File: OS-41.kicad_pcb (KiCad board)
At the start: 4 copper layers, 45.2 x 55.8 mm, 74 parts, among them J1 Conn_01x02_Pin, J2 Conn_01x02_Pin, J3 Conn_01x02_Pin, J4 Conn_Coaxial, J5 Conn_01x02_Pin, J6 USB_B_Micro, J7 Conn_01x09_Pin, SW2 TS-1187A-B-A-B, SW3 TS-1187A-B-A-B, U1 GPS1003, U10 W25Q128JVS, U2 SI4432-B1-FMR, U3 MCP1640x-xCHY, U4 ATGM336H-5N31, U5 DS18B20, U6 BMP390L, U7 RP2040, U8 ABM8-272-T3_C20625731, U9 AMS1117-3.3, X1 SMD-3225_4P 30.000MHZ 10PF

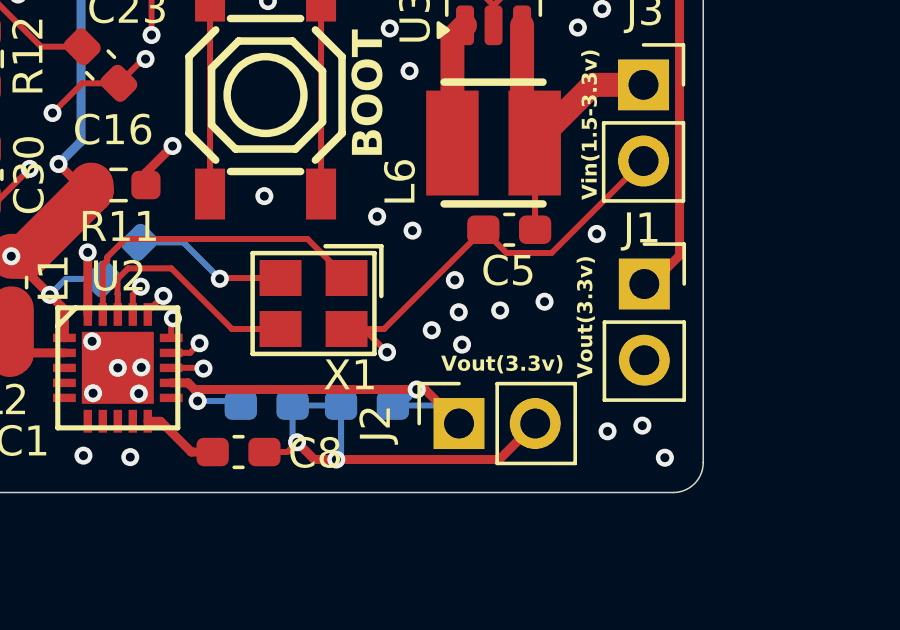
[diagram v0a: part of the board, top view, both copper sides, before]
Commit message: add polarity
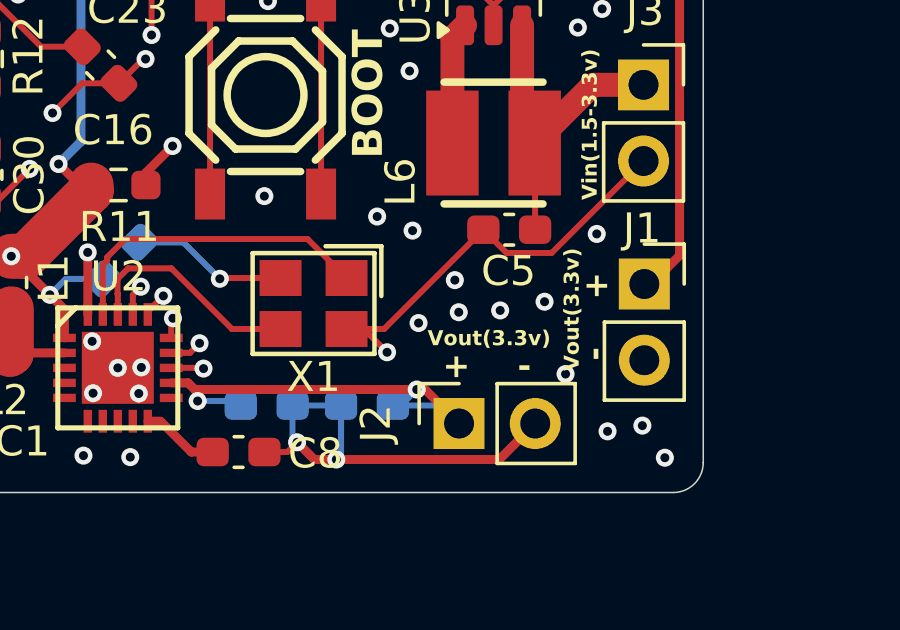
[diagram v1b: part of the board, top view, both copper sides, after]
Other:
- board text added: "+"
- board text added: "-"
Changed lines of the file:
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@@
 		(at 125 122.15 180)
 		(property "Reference" "X1"
-			(at -1.225 -2.4 0)
+			(at 0 -2.45 0)
 			(layer "F.SilkS")
 			(effects
@@
 		(layer "Edge.Cuts")
 	)
+	(gr_text "+"
+		(at 132.9 115.7 0)
+		(layer "B.SilkS")
+		(effects
+			(font
+				(size 1.5 1.5)
+				(thickness 0.3)
+				(bold yes)
+			)
+			(justify left bottom)
+		)
+	)
+	(gr_text "-"
+		(at 134.8 118.5 90)
+		(layer "B.SilkS")
+		(effects
+			(font
+				(size 1.5 1.5)
+				(thickness 0.3)
+				(bold yes)
+			)
+			(justify left bottom)
+		)
+	)
 	(gr_text "G13"
 		(at 93.2 109.1 -90)
@@
 	)
 	(gr_text "Vout(3.3v)"
-		(at 129.25 124.45 0)
+		(at 128.8 123.6 0)
 		(layer "F.SilkS")
 		(effects
@@
 	)
 	(gr_text "Vout(3.3v)"
-		(at 134.35 124.65 90)
+		(at 133.9 124.4 90)
 		(layer "F.SilkS")
 		(effects
@@
 		)
 	)
+	(gr_text "+"
+		(at 134 121.1 -90)
+		(layer "F.SilkS")
+		(effects
+			(font
+				(size 0.8 0.8)
+				(thickness 0.15)
+				(bold yes)
+			)
+			(justify left bottom)
+		)
+	)
 	(gr_text "G"
 		(at 104.95 111.39 0)
@@
 		)
 	)
+	(gr_text "-"
+		(at 134 123.6 -90)
+		(layer "F.SilkS")
+		(effects
+			(font
+				(size 0.8 0.8)
+				(thickness 0.15)
+				(bold yes)
+			)
+			(justify left bottom)
+		)
+	)
 	(gr_text "R"
 		(at 104.91 113.5 0)
@@
 		)
 	)
+	(gr_text "+"
+		(at 129.3 124.7 0)
+		(layer "F.SilkS")
+		(effects
+			(font
+				(size 0.8 0.8)
+				(thickness 0.15)
+				(bold yes)
+			)
+			(justify left bottom)
+		)
+	)
 	(gr_text "G12"
 		(at 93.2 106.4 -90)
@@
 		)
 	)
+	(gr_text "-"
+		(at 131.8 124.7 0)
+		(layer "F.SilkS")
+		(effects
+			(font
+				(size 0.8 0.8)
+				(thickness 0.15)
+				(bold yes)
+			)
+			(justify left bottom)
+		)
+	)
 	(gr_text "ERR"
 		(at 103.31 115.61 0)
@@
 	)
 	(via
-		(at 128.94 123.04)
+		(at 128.5 122.8)
 		(size 0.6)
 		(drill 0.3)
@@
 	)
 	(via
-		(at 129.95 123.52)
+		(at 133.4 124.5)
 		(size 0.6)
 		(drill 0.3)

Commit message: Fix some important things
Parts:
- added C15: 100nF, Capacitor_SMD:C_0603_1608Metric_Pad1.08x0.95mm_HandSolder, B.Cu at (100.8, 116.2)
- added R13: 4.7k, Resistor_SMD:R_0603_1608Metric_Pad0.98x0.95mm_HandSolder, B.Cu at (121.5, 99.1)
- added R14: 4.7k, Resistor_SMD:R_0603_1608Metric_Pad0.98x0.95mm_HandSolder, B.Cu at (123.3, 109.8)
- added R5: 10k, Resistor_SMD:R_0603_1608Metric_Pad0.98x0.95mm_HandSolder, F.Cu at (98.6, 108.4)
- R2: value 12k -> 10k
- renumbered C15 to C16, C16 to C17, C17 to C18, C18 to C19, C19 to C20, C20 to C21, C21 to C22, C22 to C23, C23 to C24, C24 to C25, C25 to C26, C26 to C27, C27 to C28, C28 to C29, C29 to C30, C30 to C31, C31 to C32, R9 to R10, R10 to R11, R11 to R12, R12 to R15, R13 to R16, R14 to R17, R5 to R6, R6 to R7, R7 to R8, R8 to R9, SW2 to SW1, SW3 to SW2
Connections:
- U7 pad 34: unconnected-(U7-GPIO22-Pad34) -> DQ
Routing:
- net DQ: track 6.00 -> 28.5 mm, vias 0 -> 2
- net VCC: track 225.5 -> 238.4 mm, vias 17 -> 18
- net SCL: track 8.61 -> 15.5 mm, vias 2 -> 3
- net RESET: track 25.8 -> 30.6 mm, vias 2 -> 3
- net GND: track 333.1 -> 337.6 mm, vias 156 -> 157
- net SDA: track 9.70 -> 11.5 mm

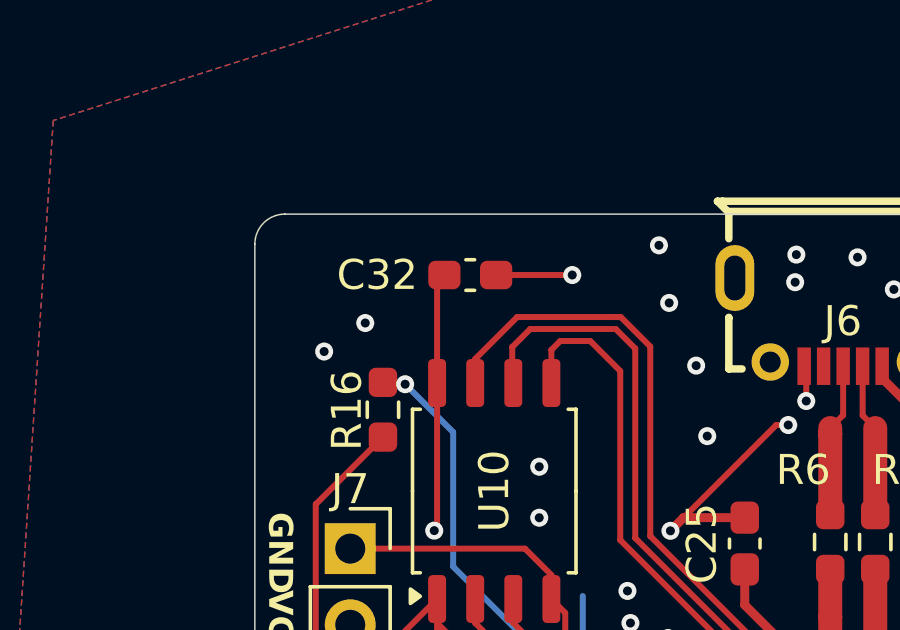
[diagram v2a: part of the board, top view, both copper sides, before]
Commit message: Rotate a capacitor
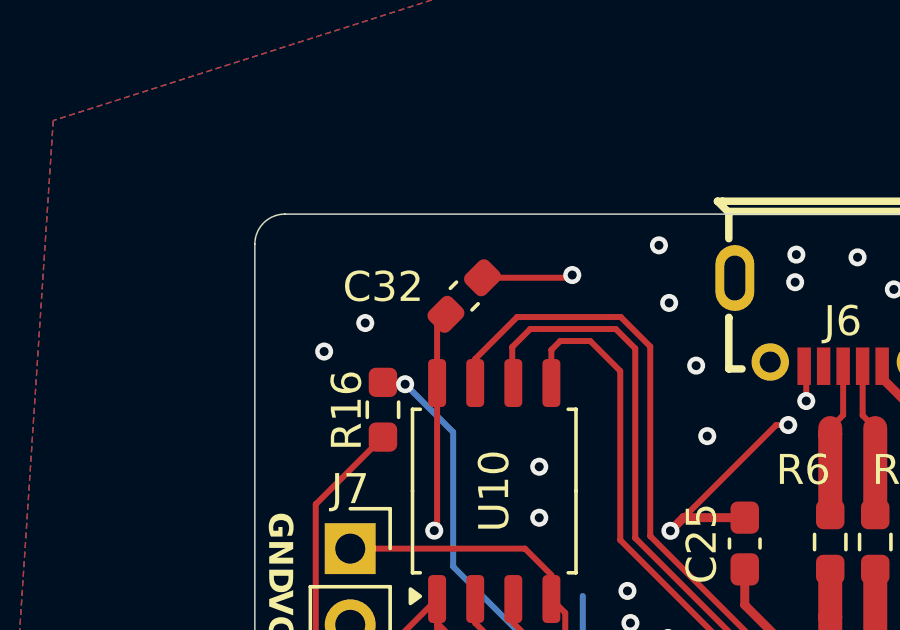
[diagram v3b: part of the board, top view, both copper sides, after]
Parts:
- moved C32 0.73 mm to (99.8, 89.1), turned to 45 degrees
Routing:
- net VCC: track 238.4 -> 237.1 mm
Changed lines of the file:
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@@
 	(footprint "Capacitor_SMD:C_0603_1608Metric_Pad1.08x0.95mm_HandSolder"
 		(layer "F.Cu")
-		(at 100 88.4)
+		(at 99.8 89.1 45)
 		(descr "Capacitor SMD 0603 (1608 Metric), square (rectangular) end terminal, IPC_7351 nominal with elongated pad for handsoldering. (Body size source: IPC-SM-782 page 76, https://www.pcb-3d.com/wordpress/wp-content/uploads/ipc-sm-782a_amendment_1_and_2.pdf), generated with kicad-footprint-generator")
 		(tags "capacitor handsolder")
 		(property "Reference" "C32"
-			(at -3.1 0 0)
+			(at -1.697056 -2.12132 0)
 			(layer "F.SilkS")
 			(effects
@@
 		)
 		(property "Value" "100nF"
-			(at 0 1.43 0)
+			(at 0 1.43 45)
 			(layer "F.Fab")
 			(effects
@@
 		)
 		(property "Footprint" "Capacitor_SMD:C_0603_1608Metric_Pad1.08x0.95mm_HandSolder"
-			(at 0 0 0)
+			(at 0 0 45)
 			(unlocked yes)
 			(layer "F.Fab")
@@
 		)
 		(property "Datasheet" ""
-			(at 0 0 0)
+			(at 0 0 45)
 			(unlocked yes)
 			(layer "F.Fab")
@@
 		)
 		(property "Description" "Unpolarized capacitor"
-			(at 0 0 0)
+			(at 0 0 45)
 			(unlocked yes)
 			(layer "F.Fab")
@@
 		)
 		(fp_text user "${REFERENCE}"
-			(at 0 0 0)
+			(at 0 0 45)
 			(layer "F.Fab")
 			(effects
@@
 		)
 		(pad "1" smd roundrect
-			(at -0.8625 0)
+			(at -0.862501 0 45)
 			(size 1.075 0.95)
 			(layers "F.Cu" "F.Paste" "F.Mask")
@@
 		)
 		(pad "2" smd roundrect
-			(at 0.8625 0)
+			(at 0.862501 0 45)
 			(size 1.075 0.95)
 			(layers "F.Cu" "F.Paste" "F.Mask")
@@
 		(tags "capacitor handsolder")
 		(property "Reference" "C15"
-			(at 0 1.43 360)
+			(at 0 1.43 0)
 			(layer "B.SilkS")
 			(effects
@@
 		)
 		(property "Value" "100nF"
-			(at 0 -1.43 360)
+			(at 0 -1.43 0)
 			(layer "B.Fab")
 			(effects
@@
 		)
 		(fp_text user "${REFERENCE}"
-			(at 0 0 360)
+			(at 0 0 0)
 			(layer "B.Fab")
 			(effects
@@
 	)
 	(segment
+		(start 100.40988 88.49012)
+		(end 103.30988 88.49012)
+		(width 0.2)
+		(layer "F.Cu")
+		(net 1)
+	)
+	(segment
 		(start 118.05 90.9)
 		(end 117.9 90.9)
@@
 	)
 	(segment
+		(start 103.30988 88.49012)
+		(end 103.4 88.4)
+		(width 0.2)
+		(layer "F.Cu")
+		(net 1)
+	)
+	(segment
 		(start 118.05 90.25)
 		(end 117.2 89.4)
@@
 	)
 	(segment
-		(start 100.8625 88.4)
-		(end 103.4 88.4)
-		(width 0.2)
-		(layer "F.Cu")
-		(net 1)
-	)
-	(segment
 		(start 131 112.212501)
 		(end 131 112.875)
@@
 	)
 	(segment
-		(start 98.895 88.6425)
-		(end 99.1375 88.4)
-		(width 0.2)
-		(layer "F.Cu")
-		(net 2)
-	)
-	(segment
 		(start 126.062501 108.2)
 		(end 126.9 107.362501)
@@
 	)
 	(segment
-		(start 98.895 92)
-		(end 98.895 88.6425)
-		(width 0.2)
-		(layer "F.Cu")
-		(net 2)
-	)
-	(segment
 		(start 117.5875 118.387502)
 		(end 117.5875 118.2)
@@
 	)
 	(segment
+		(start 98.895 92)
+		(end 98.895 90.005)
+		(width 0.2)
+		(layer "F.Cu")
+		(net 2)
+	)
+	(segment
 		(start 111.7 110.075)
 		(end 111.7 109.265822)
@@
 		(layer "F.Cu")
 		(net 2)
+	)
+	(segment
+		(start 98.895 90.005)
+		(end 99.19012 89.70988)
+		(width 0.2)
+		(layer "F.Cu")
+		(net 2)

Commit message: Fix some silkscreen issues
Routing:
- net GND: vias 157 -> 162
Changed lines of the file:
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@@
 		(tags "Through hole socket strip THT 1x09 2.54mm single row")
 		(property "Reference" "J7"
-			(at 0 -1.980001 0)
+			(at 1.7 22.179999 -90)
 			(layer "F.SilkS")
 			(effects
 				(font
-					(size 1 1)
-					(thickness 0.15)
+					(size 0.5 0.5)
+					(thickness 0.125)
 				)
 			)
@@
 		(tags "resistor handsolder")
 		(property "Reference" "R5"
-			(at 0 -1.43 90)
+			(at 0.1 -1.2 90)
 			(layer "F.SilkS")
 			(effects
@@
 	)
 	(gr_text "GPIO"
-		(at 97.76 104.7 270)
+		(at 94.6 95.9 0)
 		(layer "F.SilkS")
 		(effects
 			(font
-				(size 1 1)
-				(thickness 0.2)
+				(size 0.8 0.8)
+				(thickness 0.1)
 				(bold yes)
 			)
@@
 	)
 	(via
+		(at 104.4 87.5)
+		(size 0.6)
+		(drill 0.3)
+		(layers "F.Cu" "B.Cu")
+		(free yes)
+		(net 1)
+	)
+	(via
 		(at 135.5 93)
 		(size 0.6)
@@
 	)
 	(via
+		(at 102.4 87.5)
+		(size 0.6)
+		(drill 0.3)
+		(layers "F.Cu" "B.Cu")
+		(free yes)
+		(net 1)
+	)
+	(via
 		(at 127.5 96)
 		(size 0.6)
@@
 	)
 	(via
+		(at 94.2 93.2)
+		(size 0.6)
+		(drill 0.3)
+		(layers "F.Cu" "B.Cu")
+		(free yes)
+		(net 1)
+	)
+	(via
 		(at 111.2 92.6)
 		(size 0.6)
@@
 	)
 	(via
+		(at 94.2 89.4)
+		(size 0.6)
+		(drill 0.3)
+		(layers "F.Cu" "B.Cu")
+		(free yes)
+		(net 1)
+	)
+	(via
 		(at 132.5 93)
 		(size 0.6)
@@
 		(net 1)
 	)
+	(via
+		(at 94.4 87.6)
+		(size 0.6)
+		(drill 0.3)
+		(layers "F.Cu" "B.Cu")
+		(free yes)
+		(net 1)
+	)

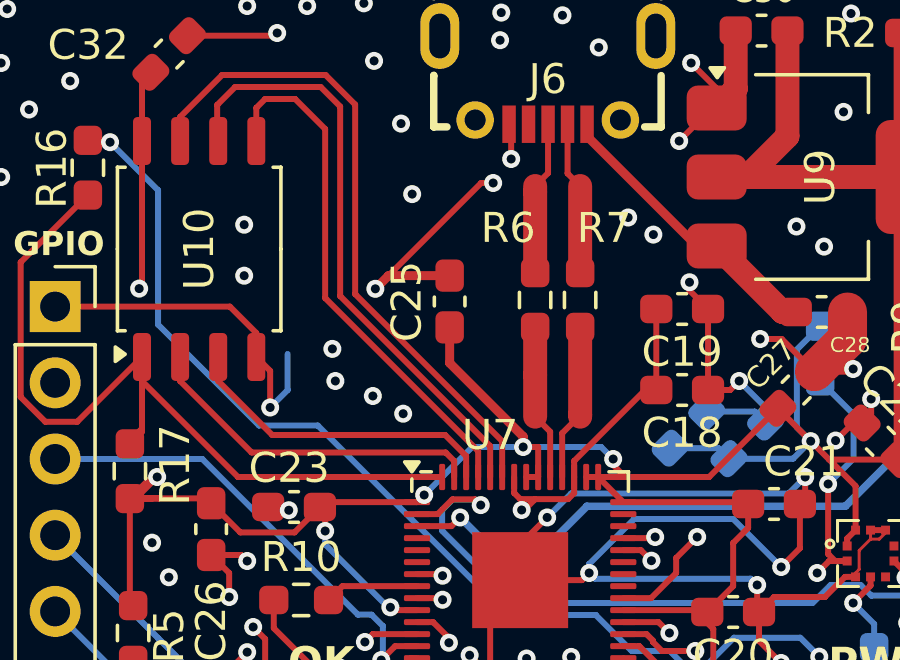
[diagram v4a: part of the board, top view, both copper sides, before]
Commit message: Add silkscreen graphics
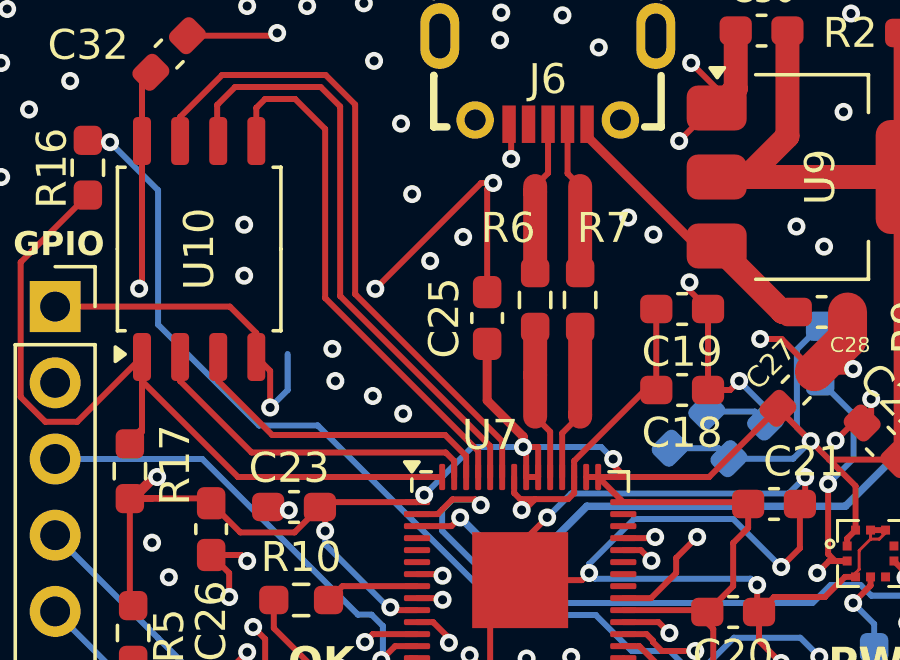
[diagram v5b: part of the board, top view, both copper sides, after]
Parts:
- added G***: LOGO, LOGO, B.Cu at (116.7, 106.8)
- moved C25 1.37 mm to (110.4, 97.9)
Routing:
- net GND: track 338.1 -> 339.2 mm, vias 162 -> 164
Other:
- board text added: "Micro USB Program + Debug"

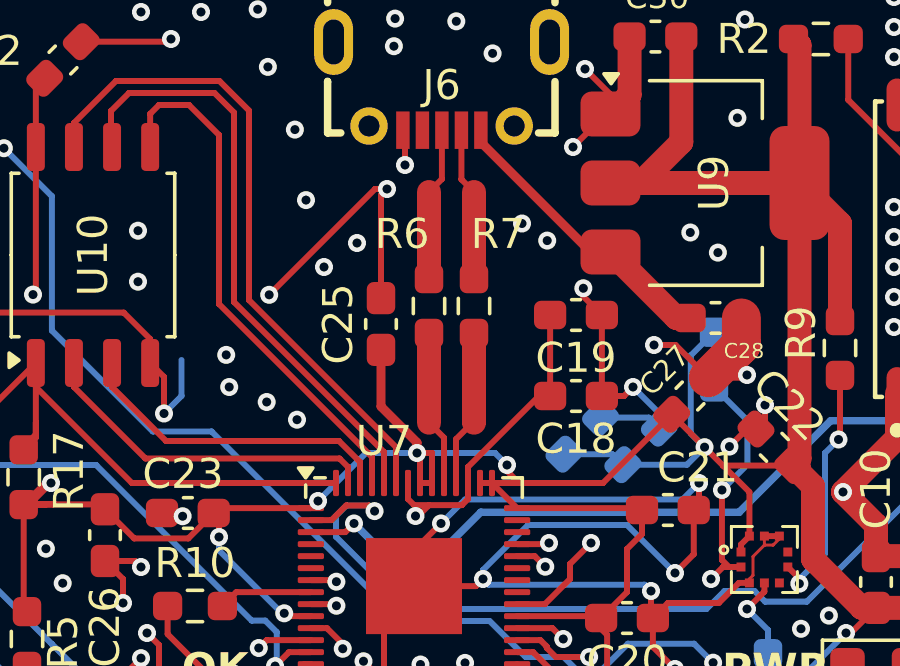
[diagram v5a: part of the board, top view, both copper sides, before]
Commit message: Place USB resistors closer to chip
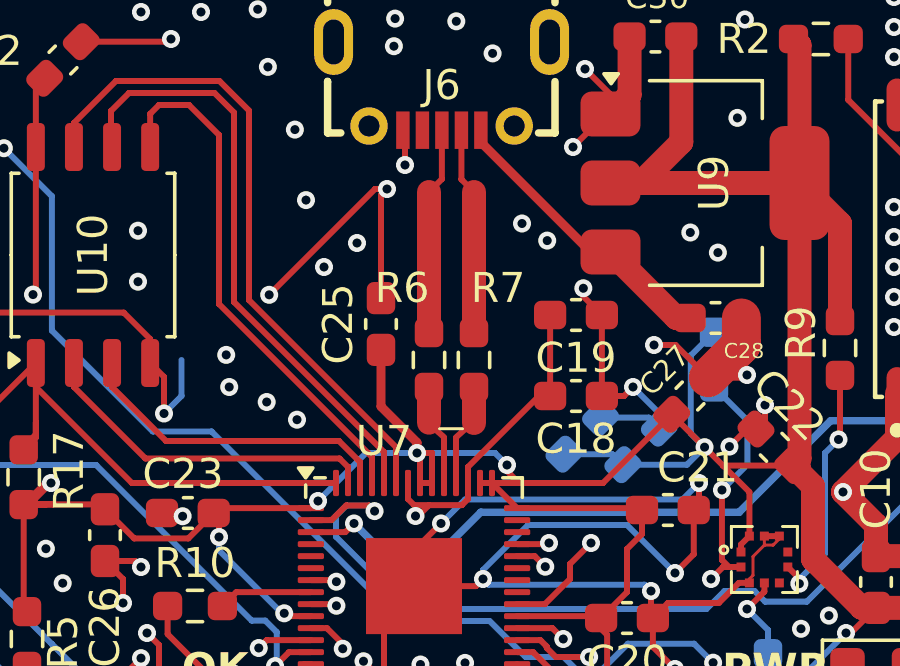
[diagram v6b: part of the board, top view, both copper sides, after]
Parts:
- moved R6 1.80 mm to (112.0, 99.1)
- moved R7 1.80 mm to (113.5, 99.1)
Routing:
- net USB_P: track 5.19 -> 2.69 mm
- net USB_N: track 5.27 -> 2.80 mm
- net D-: track 5.12 -> 6.92 mm
- net D+: track 5.13 -> 6.93 mm
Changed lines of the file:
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@@
 	(footprint "Resistor_SMD:R_0603_1608Metric_Pad0.98x0.95mm_HandSolder"
 		(layer "F.Cu")
-		(at 112 97.3 -90)
+		(at 112 99.1 -90)
 		(descr "Resistor SMD 0603 (1608 Metric), square (rectangular) end terminal, IPC_7351 nominal with elongated pad for handsoldering. (Body size source: IPC-SM-782 page 72, https://www.pcb-3d.com/wordpress/wp-content/uploads/ipc-sm-782a_amendment_1_and_2.pdf), generated with kicad-footprint-generator")
 		(tags "resistor handsolder")
@@
 	(footprint "Resistor_SMD:R_0603_1608Metric_Pad0.98x0.95mm_HandSolder"
 		(layer "F.Cu")
-		(at 113.5 97.3 90)
+		(at 113.5 99.1 90)
 		(descr "Resistor SMD 0603 (1608 Metric), square (rectangular) end terminal, IPC_7351 nominal with elongated pad for handsoldering. (Body size source: IPC-SM-782 page 72, https://www.pcb-3d.com/wordpress/wp-content/uploads/ipc-sm-782a_amendment_1_and_2.pdf), generated with kicad-footprint-generator")
 		(tags "resistor handsolder")
@@
 		)
 	)
+	(gr_line
+		(start 112.5 101.67)
+		(end 112.15 101.36)
+		(stroke
+			(width 0.2)
+			(type default)
+		)
+		(layer "F.Cu")
+		(net 42)
+	)
+	(gr_line
+		(start 112.9 101.68)
+		(end 113.33 101.29)
+		(stroke
+			(width 0.2)
+			(type default)
+		)
+		(layer "F.Cu")
+		(net 43)
+	)
+	(gr_line
+		(start 112.35 101.39)
+		(end 113.12 101.39)
+		(stroke
+			(width 0.1)
+			(type default)
+		)
+		(layer "F.SilkS")
+	)
 	(gr_arc
 		(start 92.82 87.37)
@@
 	)
 	(segment
-		(start 112 96.3875)
-		(end 112 93.699999)
-		(width 0.8)
-		(layer "F.Cu")
-		(net 16)
-	)
-	(segment
-		(start 112 93.699999)
-		(end 112 93.5)
-		(width 0.8)
-		(layer "F.Cu")
-		(net 16)
-	)
-	(segment
 		(start 112.429999 91.44)
 		(end 112.429999 93.070001)
@@
 	)
 	(segment
-		(start 113.5 96.3875)
-		(end 113.5 93.5)
+		(start 112 93.5)
+		(end 112 98.1875)
 		(width 0.8)
 		(layer "F.Cu")
-		(net 17)
+		(net 16)
 	)
 	(segment
@@
 	)
 	(segment
+		(start 113.5 93.5)
+		(end 113.5 98.1875)
+		(width 0.8)
+		(layer "F.Cu")
+		(net 17)
+	)
+	(segment
 		(start 113.079999 91.439999)
 		(end 113.079999 93.079999)
@@
 	)
 	(segment
-		(start 112.5 101.68934)
-		(end 112 101.18934)
+		(start 112.5 103.2)
+		(end 112.5 101.68934)
 		(width 0.2)
 		(layer "F.Cu")
@@
 	)
 	(segment
-		(start 112 98.2125)
-		(end 112 99.800001)
-		(width 0.8)
-		(layer "F.Cu")
-		(net 42)
-	)
-	(segment
-		(start 112 99.800001)
+		(start 112 100.0125)
 		(end 112 101.18934)
 		(width 0.8)
@@
 	)
 	(segment
-		(start 112.5 103.2)
-		(end 112.5 101.68934)
-		(width 0.2)
-		(layer "F.Cu")
-		(net 42)
-	)
-	(segment
-		(start 112.9 101.74)
-		(end 113.45 101.19)
+		(start 112.9 101.7)
+		(end 112.9 101.69)
 		(width 0.2)
 		(layer "F.Cu")
@@
 	)
 	(segment
-		(start 113.5 98.2125)
-		(end 113.5 101.12)
-		(width 0.8)
+		(start 112.9 101.7)
+		(end 112.9 103.2)
+		(width 0.2)
 		(layer "F.Cu")
 		(net 43)
 	)
 	(segment
-		(start 113.5 101.12)
-		(end 113.5 101.19)
+		(start 113.5 100.0125)
+		(end 113.5 101.2)
 		(width 0.8)
 		(layer "F.Cu")
@@
 	)
 	(segment
-		(start 113.45 101.19)
-		(end 113.5 101.19)
-		(width 0.2)
-		(layer "F.Cu")
-		(net 43)
-	)
-	(segment
-		(start 112.9 103.2)
-		(end 112.9 101.74)
+		(start 113.4 101.2)
+		(end 113.5 101.2)
 		(width 0.2)
 		(layer "F.Cu")
